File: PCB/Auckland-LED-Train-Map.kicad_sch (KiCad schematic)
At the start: 173 parts, among them U3 Connector, USB-TYPE-C-16P, U4 ESP32-C3FH4, X1 40MHz, 15pF

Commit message: Long Version Checkpoint
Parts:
- removed C1, C18, C22, C8: 4.7uF, PCM_JLCPCB:C_0402, symbol PCM_JLCPCB-Capacitors:0402,4.7uF
- removed C10: 2.7pF, PCM_JLCPCB:C_0402, symbol PCM_JLCPCB-Capacitors:0402,2.7pF
- removed C13: 1pF, PCM_JLCPCB:C_0402, symbol PCM_JLCPCB-Capacitors:0402,1pF
- removed C14: 22uF, PCM_JLCPCB:C_0603, symbol PCM_JLCPCB-Capacitors:0603,22uF
- removed C17: 100nF, PCM_JLCPCB:C_0402, symbol PCM_JLCPCB-Capacitors:0402,100nF
- removed C19: 10uF, PCM_JLCPCB:C_0402, symbol PCM_JLCPCB-Capacitors:0402,10uF
- removed C9: 4.7pF, PCM_JLCPCB:C_0402, symbol PCM_JLCPCB-Capacitors:0402,4.7pF
- removed D10, D100, D101, D102, D103, D104, D11, D12, D13, D14, D15, D16, D17, D18, D19, D2, D20, D200, D201, D202, D203, D204, D205, D206, D207, D208, D209, D21, D210, D211, D212, D213, D214, D215, D216, D217, D218, D22, D23, D24, D25, D26, D27, D28, D29, D3, D30, D31, D32, D33, D34, D35, D36, D37, D38, D39, D4, D40, D41, D42, D43, D44, D45, D46, D47, D48, D49, D5, D50, D51, D52, D53, D54, D55, D56, D57, D58, D59, D6, D60, D61, D62, D63, D64, D65, D66, D67, D68, D69, D7, D70, D71, D72, D73, D74, D75, D76, D77, D78, D79, D8, D80, D81, D82, D83, D84, D85, D86, D87, D88, D89, D9, D90, D91, D92, D93, D94, D95, D96, D97, D98, D99: WS2812B, PCM_JLCPCB:LED-SMD_4P-L1.6-W1.5_XL-1615RGBC-WS2812B, symbol PCM_JLCPCB-Extended:LED, WS2812B, 1615
- removed R1: 510Ω, PCM_JLCPCB:R_0402, symbol PCM_JLCPCB-Resistors:0402,510Ω
- removed R10: 47kΩ, PCM_JLCPCB:R_0402, symbol PCM_JLCPCB-Resistors:0402,47kΩ
- removed R11: 1kΩ, PCM_JLCPCB:R_0402, symbol PCM_JLCPCB-Resistors:0402,1kΩ
- removed R12: 68kΩ, PCM_JLCPCB:R_0402, symbol PCM_JLCPCB-Resistors:0402,68kΩ
- removed R13: 15kΩ, PCM_JLCPCB:R_0402, symbol PCM_JLCPCB-Resistors:0402,15kΩ
- removed R5: 0Ω, PCM_JLCPCB:R_0402, symbol PCM_JLCPCB-Resistors:0402,0Ω
- removed RT1: 47kΩ,4050, JLCPCB-Kicad-Footprints:RT_0402, symbol JLCPCB-Variable-Resistors:NTC,47kΩ,4050,0402
- added C1: 10uF, PCM_JLCPCB:C_0603, symbol PCM_JLCPCB-Capacitors:0603,10uF
- added C2, C21, C22, C6: 100nF, PCM_JLCPCB:C_0402, symbol PCM_JLCPCB-Capacitors:0402,100nF
- added C23, C26, C29, C32, C4, C5, C7: 10uF, PCM_JLCPCB:C_0402, symbol PCM_JLCPCB-Capacitors:0402,10uF
- added C24, C25, C27, C28, C30, C31, C33, C34: 220nF, PCM_JLCPCB:C_0402, symbol PCM_JLCPCB-Capacitors:0402,220nF
- added C35: 1uF, PCM_JLCPCB:C_0402, symbol PCM_JLCPCB-Capacitors:0402,1uF
- added C36, C37: 1.5pF, PCM_JLCPCB:C_0402, symbol PCM_JLCPCB-Capacitors:0402,1.5pF
- added D1: MMSZ5227B, PCM_JLCPCB:D_SOD-123, symbol PCM_JLCPCB-Diodes:Zener,MMSZ5227B
- added D3: SRV05-4A, PCM_JLCPCB:SOT-23-6_L2.9-W1.6-P0.95-LS2.9-BL, symbol PCM_JLCPCB-Diode-Packages:Package, SRV05-4A_C20615829
- added D4, D5: MM1W5V6, PCM_JLCPCB:D_SOD-123, symbol PCM_JLCPCB-Diodes:Zener,MM1W5V6
- added D6, D7: SS54, PCM_JLCPCB:D_SMA, symbol PCM_JLCPCB-Diodes:Schottky,SS54
- added F1: Polyfuse, Fuse:Fuse_0805_2012Metric_Pad1.15x1.40mm_HandSolder, symbol Device:Polyfuse
- added J1: Conn_01x06_Socket, Connector_PinHeader_2.54mm:PinHeader_1x06_P2.54mm_Vertical, symbol Connector:Conn_01x06_Socket
- added Q1: HL3415A, PCM_JLCPCB:Q_SOT-23, symbol PCM_JLCPCB-Transistors:PMOS,HL3415A
- added Q2: MMBT3904, PCM_JLCPCB:Q_SOT-23, symbol PCM_JLCPCB-Transistors:NPN,MMBT3904
- added R10, R15: 100Ω, PCM_JLCPCB:R_0402, symbol PCM_JLCPCB-Resistors:0402,100Ω
- added R11: 0Ω, PCM_JLCPCB:R_0402, symbol PCM_JLCPCB-Resistors:0402,0Ω
- added R16: 100kΩ, PCM_JLCPCB:R_0402, symbol PCM_JLCPCB-Resistors:0402,100kΩ
- added R17: 10kΩ, PCM_JLCPCB:R_0402, symbol PCM_JLCPCB-Resistors:0402,10kΩ
- added R18: 1kΩ, PCM_JLCPCB:R_0402, symbol PCM_JLCPCB-Resistors:0402,1kΩ
- added R19, R20: 5.1kΩ, PCM_JLCPCB:R_0402, symbol PCM_JLCPCB-Resistors:0402,5.1kΩ
- added R21, R8: 0Ω, PCM_JLCPCB:R_1206, symbol PCM_JLCPCB-Resistors:1206,0Ω
- added R7: 750Ω, PCM_JLCPCB:R_1206, symbol PCM_JLCPCB-Resistors:1206,750Ω
- added TP1: NAL-NIMT_LED, Custom_Footprints:TestPoint_Pad_D2.0mm, symbol Connector:TestPoint
- added TP2: NAL-NIMT_MCU, Custom_Footprints:TestPoint_Pad_D2.0mm, symbol Connector:TestPoint
- added TP3: STRAND-MNK_MCU, Custom_Footprints:TestPoint_Pad_D2.0mm, symbol Connector:TestPoint
- added TP4: STRAND-MNK_LED, Custom_Footprints:TestPoint_Pad_D2.0mm, symbol Connector:TestPoint
- added TP5: PMOS_Gate, Custom_Footprints:TestPoint_Pad_D2.0mm, symbol Connector:TestPoint
- added TP6: LED_+5V, Custom_Footprints:TestPoint_Pad_D2.0mm, symbol Connector:TestPoint
- added TP7: NPN_Gate, Custom_Footprints:TestPoint_Pad_D2.0mm, symbol Connector:TestPoint
- added U1: XC6206P332MR, PCM_JLCPCB:SOT-23-3_L2.9-W1.6-P1.90-LS2.8-BR, symbol PCM_JLCPCB-Power:LDO, 3.3V, 0.2A
- added U3: SN74LVC4245APWR, PCM_JLCPCB:TSSOP-24_L7.8-W4.4-P0.65-LS6.4-BL, symbol PCM_JLCPCB-ICs:Level Shifter, 8 Channel, TSN74LVC4245APWR
- added U5: Connector, USB-TYPE-C-16P, PCM_JLCPCB:TYPE-C-SMD_HX-TYPE-C-16PIN, symbol PCM_JLCPCB-Extended:Connector, USB-TYPE-C-16P
- AE1: footprint Inverted_F_Antenna_2.4Ghz_1.0mmPCB_TI_CC2430DB:Inverted_F_Antenna_2.4Ghz_1.0mmPCB_TI_CC2430DB.pretty -> Custom_Footprints:Inverted_F_Antenna_2.4Ghz_1.0mmPCB_TI_CC2430DB.pretty
- C10: renamed from C2; Stock 21965782 -> 20577604
- C11: renamed from C3; Stock 21965782 -> 20577604
- C12: renamed from C5; Stock 2758866 -> 2162276
- C13: renamed from C6; Stock 7581604 -> 6607844
- C14: renamed from C12; Stock 21965782 -> 20577604
- C18: renamed from C4; Stock 7581604 -> 6607844
- C19: renamed from C15; Stock 727564 -> 680404
- C20: renamed from C16; Stock 727564 -> 680404
- C3: renamed from C21; Stock 21965782 -> 20577604
- C8: renamed from C7; Stock 3016191 -> 1595146
- C9: renamed from C11; Stock 21965782 -> 20577604
- D2: renamed from D1; Stock 2247940 -> 2161099
- FB1: Stock 155765 -> 233758
- L1: renamed from L3; Stock 66961 -> 55146
- L2: renamed from L4; Stock 66961 -> 55146
- R1: renamed from R8; Stock 11020501 -> 14335141
- R12: renamed from R16; Stock 652462 -> 859567
- R13: renamed from R14; Stock 2165496 -> 3549665
- R14: renamed from R15; Stock 2165496 -> 3549665
- R2: renamed from R7; Stock 11020501 -> 14335141
- R3: renamed from R2; Stock 11020501 -> 14335141
- R4: renamed from R6; Stock 4267977 -> 6150463
- R5: renamed from R3; Stock 7578144 -> 6497432
- R6: renamed from R4; Stock 7578144 -> 6497432
- R9: Stock 7578144 -> 6497432
- renumbered U4 to U2, U3 to U4
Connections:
- net +3V3: now also C22.1, C4.1, C5.1, C6.1, D1.1, U1.2 (VOUT), U3.23 (VCCB(3V)), U3.24 (VCCB(3V)); no longer C10.1, C11.1, C12.1, C13.1, U2.11 (VDD3P3_RTC), U2.17 (VDD3P3_CPU), U2.31 (VDDA), U2.32 (VDDA)
- net Antenna: now also C36.1
- net BOOT_IO9: now also J1.4 (Pin_4)
- net D+: now also D3.3 (I/O), D3.4 (I/O)
- net D-: now also D3.1 (I/O), D3.6 (I/O)
- net GND: now also C1.2, C2.2, C21.2, C22.2, C23.2, C24.2, C25.2, C26.2, C27.2, C28.2, C29.2, C30.2, C31.2, C32.2, C33.2, C34.2, C35.2, C36.2, C37.2, C4.2, C5.2, C6.2, C7.2, D1.2, D3.2 (VN), D4.2, D5.2, J1.2 (Pin_2), Q2.2 (E), R11.1, R17.2, R19.2, R20.2, U1.1 (GND), U3.11 (GND), U3.12 (GND), U3.13 (GND), U5.A12B1 (GND), U5.B12A1 (GND), U5.S1 (SHIELD)
- net MCU_RX: now also J1.5 (Pin_5), R8.2
- net MCU_TX: now also J1.6 (Pin_6), R7.1
- net Reset: now also J1.3 (Pin_3)
- net VBUS: now also C1.1, C2.1, C21.1, D3.5 (VP), D5.1, F1.2, J1.1 (Pin_1), Q1.2 (S), R16.1, U1.3 (VIN), U3.1 (VCCA(5V))
- net at AE1.1 (A), L1.2, L2.2: now also C37.1
- net at U2.28 (U0TXD): now also R7.2
- net at C8.1, C9.1, FB1.2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: now also C10.1, C11.1, U2.11 (VDD3P3_RTC), U2.17 (VDD3P3_CPU), C7.1, R21.1
- net at U2.27 (U0RXD): now also R8.1
- net NAL-NIMT_MCU: now reaches U2.8 (GPIO3)
- net NAL-NIMT_MCU: now also TP2.1, U3.21 (B1)
- net at U4.A9B4 (VBUS), U4.B9A4 (VBUS): now also D6.2; no longer D2.2
- new net: C35.1, Q2.1 (B), R18.2, TP7.1
- new net: Q1.1 (G), Q2.3 (C), R16.2, TP5.1
- new net: C12.1, C13.1, R21.2, U2.31 (VDDA), U2.32 (VDDA)
- new net: R20.1, U5.A5 (CC1)
- new net: D2.2, D6.1, D7.1, F1.1
- new net: D7.2, U5.A9B4 (VBUS), U5.B9A4 (VBUS)
- new net: R19.1, U5.B5 (CC2)
- new net: R11.2, U3.2 (DIR)
- new net: R10.2, U3.3 (A1)
- new net: R15.2, U3.10 (A8)
- new net +5V: C23.1, C24.1, C25.1, C26.1, C27.1, C28.1, C29.1, C30.1, C31.1, C32.1, C33.1, C34.1, D4.1, Q1.3 (D), TP6.1
- new net LED_+5V_EN_Active_High: R17.1, R18.1
- new net LVL_Shifter_EN_Active_Low: U3.22 (OE#)
- new net NAL-NIMT-1: R10.1, TP1.1
- new net STRAND-MNK-1: R15.1, TP4.1
- new net STRAND-MNK_MCU: TP3.1, U3.14 (B8)
- no-connect marks 4 -> 16
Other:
- added sheet NAL-NIMT-1 (NAL-NIMT-1.kicad_sch)
- added sheet STRAND-MNK-1 (STRAND-MNK-1.kicad_sch)
- note added: "3.42~3.78V"
- moved on the sheet: AE1, C14, C3, C8, H1, H2, H3, H4, PN1, R4, U4

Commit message: PCB Checkpoint
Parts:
- removed C23, C26, C29, C32, C7, C8: 10uF, PCM_JLCPCB:C_0402, symbol PCM_JLCPCB-Capacitors:0402,10uF
- removed C24, C25, C27, C28, C30, C31, C33, C34: 220nF, PCM_JLCPCB:C_0402, symbol PCM_JLCPCB-Capacitors:0402,220nF
- removed C9: 100nF, PCM_JLCPCB:C_0402, symbol PCM_JLCPCB-Capacitors:0402,100nF
- removed FB1: ~, PCM_JLCPCB:FB_0805, symbol PCM_JLCPCB-Inductors:Ferrite,0805,(2)
- removed R9: 0Ω, PCM_JLCPCB:R_0402, symbol PCM_JLCPCB-Resistors:0402,0Ω
- removed TP3: STRAND-MNK_MCU, Custom_Footprints:TestPoint_Pad_D2.0mm, symbol Connector:TestPoint
- added C15: 100nF, PCM_JLCPCB:C_0402, symbol PCM_JLCPCB-Capacitors:0402,100nF
- added C7: 1uF, PCM_JLCPCB:C_0402, symbol PCM_JLCPCB-Capacitors:0402,1uF
- added L3, L4: 3.9nH,300mA, PCM_JLCPCB:L_0402, symbol PCM_JLCPCB-Inductors:3.9nH,300mA
- added L5: 15nH,300mA, PCM_JLCPCB:L_0402, symbol PCM_JLCPCB-Inductors:15nH,300mA
- added TP8: STRAND-MNK_MCU, Custom_Footprints:TestPoint_Pad_D2.0mm, symbol Connector:TestPoint
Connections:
- net +3V3: now also L3.1, L4.1
- net GND: now also C15.2, C7.2
- net STRAND-MNK_MCU: now also U3.17 (B5), TP8.1; no longer U3.14 (B8)
- net at C10.1, C11.1, R21.1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: now also C15.1, C7.1, L3.2, L4.2
- net at U2.30 (XTAL_P): now also L5.2
- net at R15.2: now also U3.7 (A5); no longer U3.10 (A8)
- net at C20.1, X1.1 (OSC): now also L5.1
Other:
- moved on the sheet: R15

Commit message: - Remove JLCPCB Outputs - V1 RC1
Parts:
- removed R21, R8: 0Ω, PCM_JLCPCB:R_1206, symbol PCM_JLCPCB-Resistors:1206,0Ω
- removed R7: 750Ω, PCM_JLCPCB:R_1206, symbol PCM_JLCPCB-Resistors:1206,750Ω
- added C16: 100nF, PCM_JLCPCB:C_0402, symbol PCM_JLCPCB-Capacitors:0402,100nF
- added C8: 10uF, PCM_JLCPCB:C_0402, symbol PCM_JLCPCB-Capacitors:0402,10uF
- added D8, D9: Green, PCM_JLCPCB:D_0805, symbol PCM_JLCPCB-Diodes:LED,0805,Green
- added R22, R9: 47kΩ, PCM_JLCPCB:R_0402, symbol PCM_JLCPCB-Resistors:0402,47kΩ
- added R7: 510Ω, PCM_JLCPCB:R_0402, symbol PCM_JLCPCB-Resistors:0402,510Ω
- added S1, S2, S3: Tactile Button, 160gf, PCM_JLCPCB:SW-SMD_4P-L5.1-W5.1-P3.70-LS6.5-TL-2, symbol PCM_JLCPCB-Connectors_Buttons:Tactile Button, 160gf
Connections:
- net +3V3: now also C10.1, C11.1, C12.1, C13.1, U2.11 (VDD3P3_RTC), U2.17 (VDD3P3_CPU), U2.31 (VDDA), U2.32 (VDDA), C8.1, D8.2
- net GND: now also C16.2, C8.2, R22.2, R9.2, S1.3 (C), S1.4 (D), S2.3 (C), S2.4 (D), S3.3 (C), S3.4 (D)
- net LVL_Shifter_EN_Active_Low: now also U2.8 (GPIO3)
- net MCU_RX: now also U2.27 (U0RXD)
- net MCU_TX: now also R7.1
- net NAL-NIMT_MCU: now also U2.9 (MTMS); no longer U2.8 (GPIO3)
- net STRAND-MNK_MCU: now also U2.10 (MTDI)
- net VDD_SPI: now also C16.1
- net MODE_BUTTON: now reaches R2.2, U2.14 (GPIO8)
- net MODE_BUTTON: now also S1.1 (A), S1.2 (B)
- net at C15.1, C7.1, L3.2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: no longer C10.1, C11.1, U2.11 (VDD3P3_RTC), U2.17 (VDD3P3_CPU)
- net -BRIGHTNESS_BUTTON: now reaches U2.12 (MTCK)
- net -BRIGHTNESS_BUTTON: now also S3.1 (A), S3.2 (B)
- net +BRIGHTNESS_BUTTON: now reaches U2.13 (MTDO)
- net +BRIGHTNESS_BUTTON: now also S2.1 (A), S2.2 (B)
- net WIFI_LED: now reaches U2.16 (GPIO10)
- net WIFI_LED: now also D9.2
- net at U2.28 (U0TXD): now also R7.2
- new net: D9.1, R22.1
- new net: D8.1, R9.1
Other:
- note added: "Power"
- moved on the sheet: C6, L3, L4, R1, R2, R3

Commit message: - V1 RC2 - Add icons
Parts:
- added C9: 10uF, PCM_JLCPCB:C_0402, symbol PCM_JLCPCB-Capacitors:0402,10uF
- added D10, D11: Red, PCM_JLCPCB:D_0805, symbol PCM_JLCPCB-Diodes:LED,0805,Red
- added D12: Green, PCM_JLCPCB:D_0805, symbol PCM_JLCPCB-Diodes:LED,0805,Green
- added R21, R8: 15kΩ, PCM_JLCPCB:R_0402, symbol PCM_JLCPCB-Resistors:0402,15kΩ
- added R23: 47kΩ, PCM_JLCPCB:R_0402, symbol PCM_JLCPCB-Resistors:0402,47kΩ
- D2: footprint PCM_JLCPCB:D_0603 -> PCM_JLCPCB:D_0805; symbol PCM_JLCPCB-Diodes:LED,0603,Red -> PCM_JLCPCB-Diodes:LED,0805,Red; Category Optocouplers & LEDs & Infrared,Light Emitting Diodes (LED) -> Optoelectronics,Light Emitting Diodes (LED); Diode Configuration (none) -> Independent Diode; Dominant Wavelength (none) -> 615nm~630nm; Emitted Color (none) -> Red; Forward Current (none) -> 25mA; Forward Voltage (VF) (none) -> 1.6V~2.6V; LCSC C2286 -> C84256; Lens Color (none) -> Colorless Transparent Lens; Luminous Intensity (none) -> 67mcd~195mcd; Manufacturer Hubei KENTO Elec -> Foshan NationStar Optoelectronics; Operating Temperature (none) -> -30°C~+85°C; Part KT-0603R -> NCD0805R1; Power Dissipation (none) -> 65mW; Price 0.009USD -> 0.016USD; Stock 2161099 -> 3045161; Viewing Angle (none) -> 130°
- R12: value 3.3kΩ -> 15kΩ; symbol PCM_JLCPCB-Resistors:0402,3.3kΩ -> PCM_JLCPCB-Resistors:0402,15kΩ; LCSC C25890 -> C25756; Part 0402WGF3301TCE -> 0402WGF1502TCE; Resistance 3.3kΩ -> 15kΩ; Stock 859567 -> 534593
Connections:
- net +3V3: now also C9.1
- net GND: now also U3.10 (A8), U3.14 (B8), U3.15 (B7), U3.16 (B6), U3.17 (B5), U3.18 (B4), U3.19 (B3), U3.5 (A3), U3.6 (A4), U3.7 (A5), U3.8 (A6), U3.9 (A7), C9.2, D10.2, D11.2, R23.2
- net LED_+5V_EN_Active_High: now also U2.9 (MTMS)
- net LVL_Shifter_EN_Active_Low: now also U2.4 (GPIO0/XTAL_32K_P); no longer U2.8 (GPIO3)
- net NAL-NIMT_MCU: now also U2.8 (GPIO3), U3.20 (B2); no longer U2.9 (MTMS), U3.21 (B1)
- net STRAND-MNK_MCU: now also U2.5 (GPIO1/XTAL_32K_N), U3.21 (B1); no longer U2.10 (MTDI), U3.17 (B5)
- net WIFI_LED: now also R8.1
- net at R10.2: now also U3.4 (A2); no longer U3.3 (A1)
- net at R15.2: now also U3.3 (A1); no longer U3.7 (A5)
- net BOOT_IO9 renamed BOOT_IO9_BUTTON
- net BOOT_IO9_BUTTON: now also S1.1 (A), S1.2 (B)
- net MODE_BUTTON: no longer names the net of R2.2, U2.14 (GPIO8)
- net MODE_BUTTON: no longer S1.1 (A), S1.2 (B)
- new net: D12.1, R23.1
- new net: D10.1, R8.2
- new net: D11.1, R21.2
- new net CONFIG_LED: D12.2, R21.1, U2.10 (MTDI)
- no-connect marks 16 -> 14
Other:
- note removed: "Power"
- moved on the sheet: AE1, C1, C10, C11, C12, C13, C14, C15, C16, C18, C19, C2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

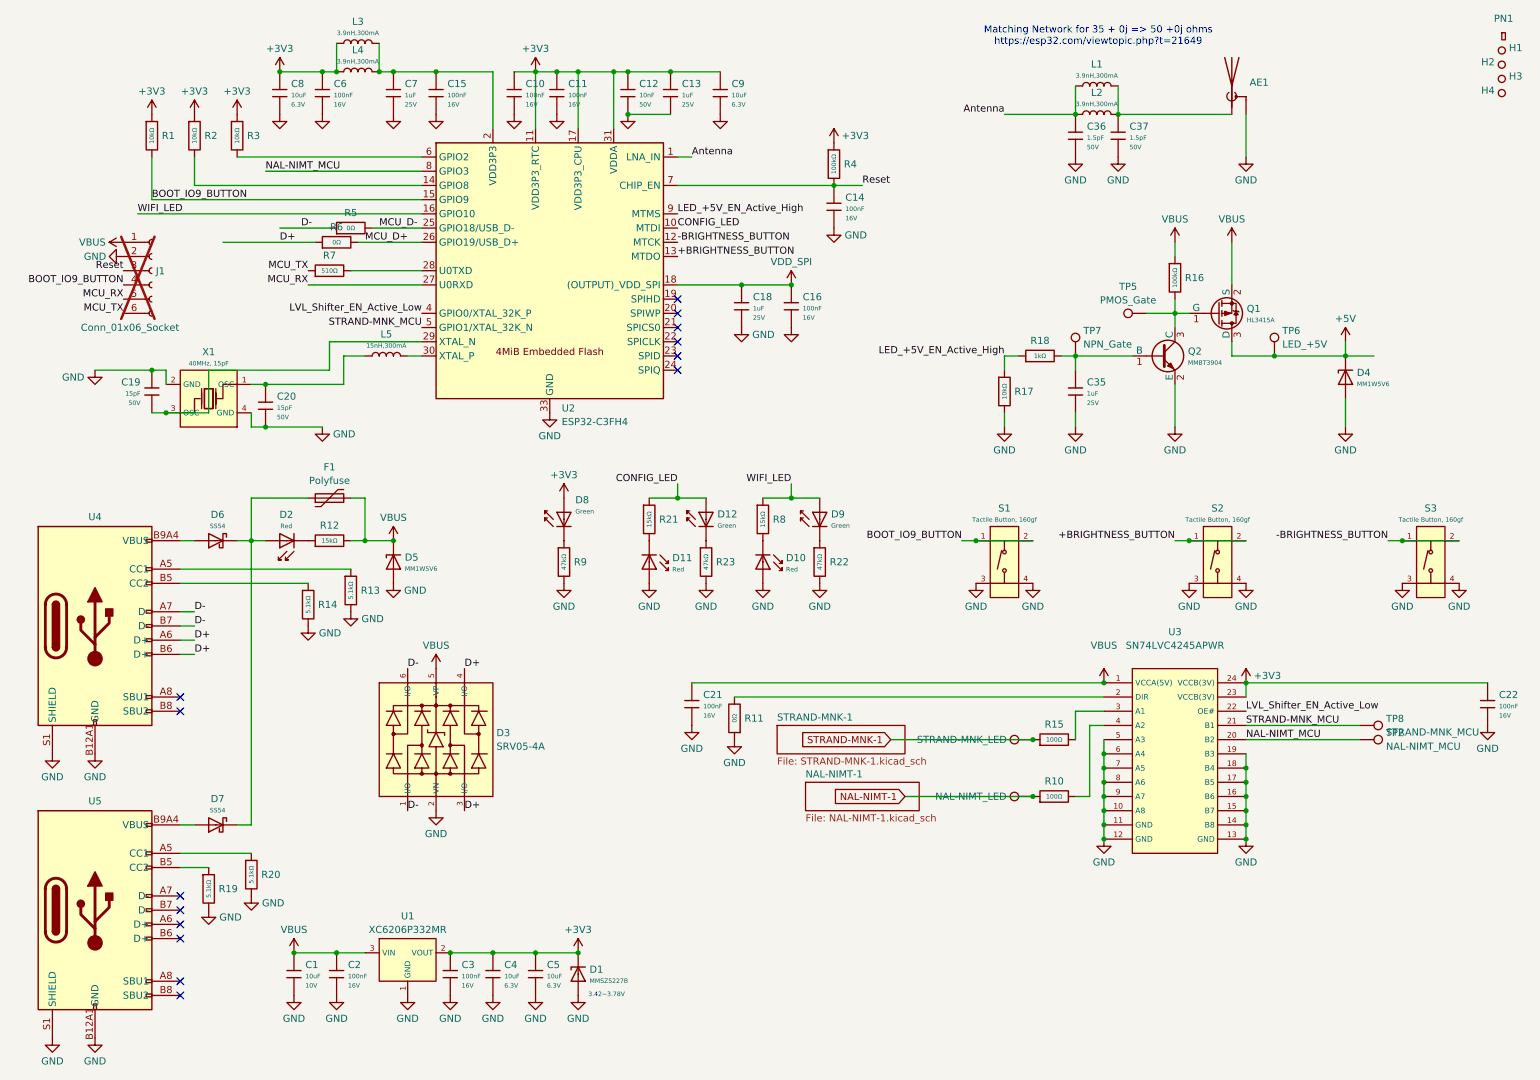
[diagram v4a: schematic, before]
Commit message: - Add Readme - V1 RC3 PCB - Tidy up Schematic - Add Datasheets
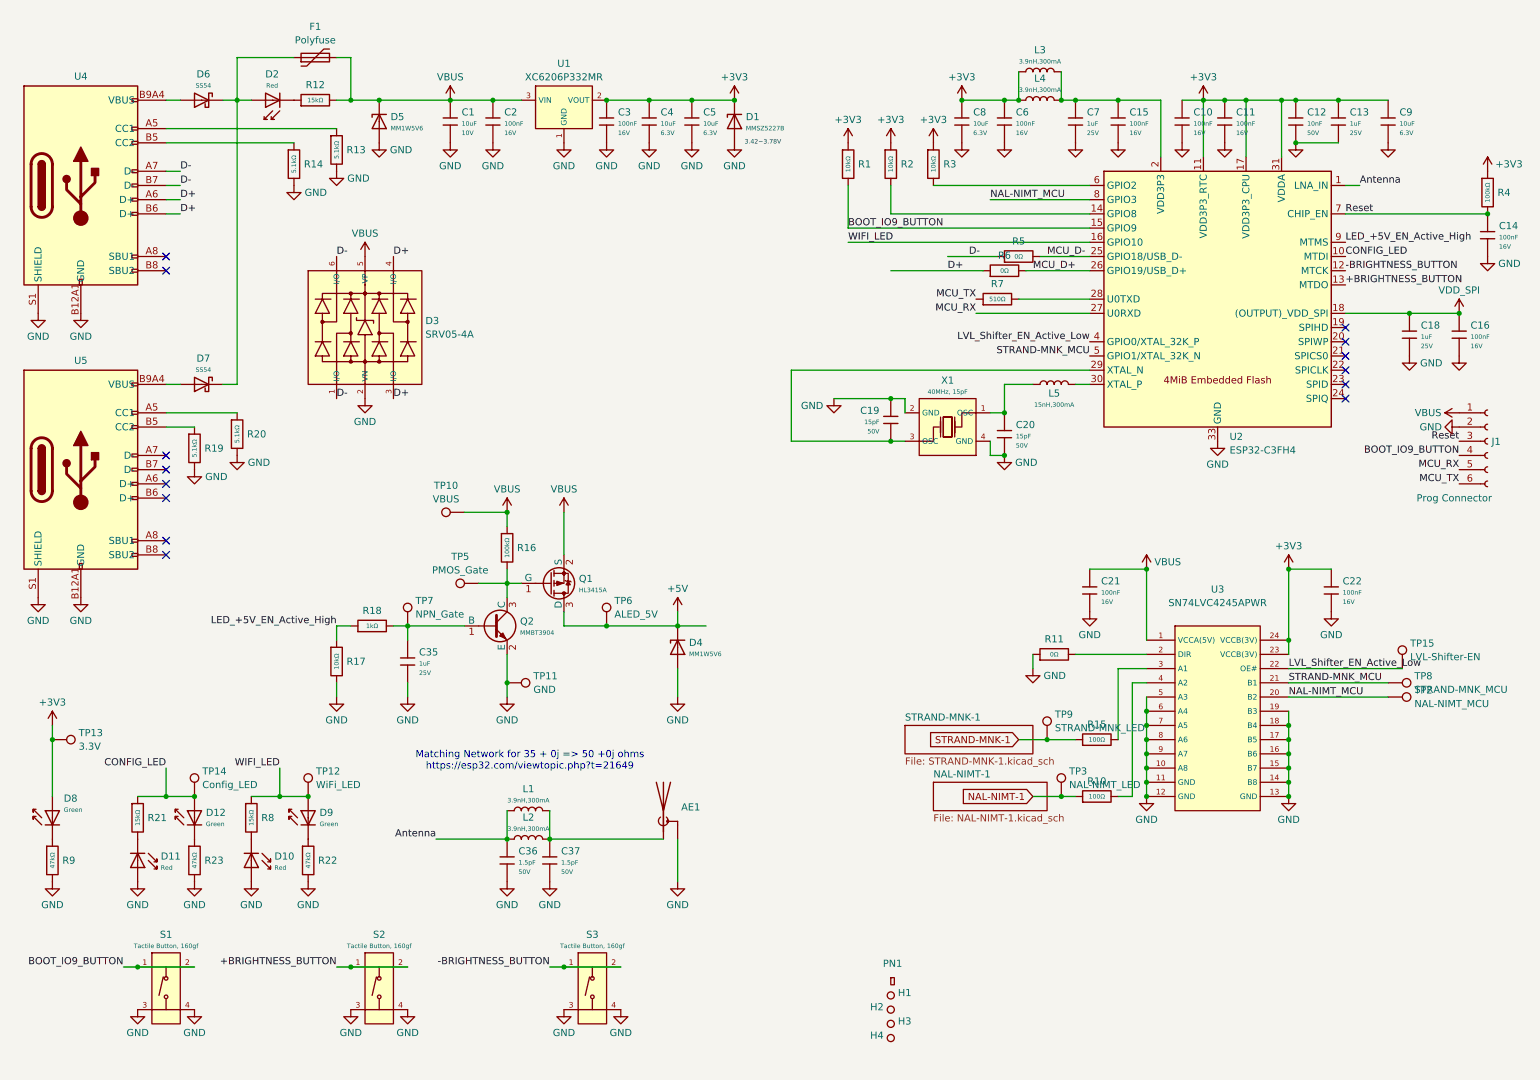
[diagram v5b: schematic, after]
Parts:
- removed TP1: NAL-NIMT_LED, Custom_Footprints:TestPoint_Pad_D2.0mm, symbol Connector:TestPoint
- removed TP4: STRAND-MNK_LED, Custom_Footprints:TestPoint_Pad_D2.0mm, symbol Connector:TestPoint
- added TP10: VBUS, Custom_Footprints:TestPoint_Pad_D1.0mm, symbol Connector:TestPoint
- added TP11: GND, Custom_Footprints:TestPoint_Pad_D1.0mm, symbol Connector:TestPoint
- added TP12: WiFi_LED, Custom_Footprints:TestPoint_Pad_D1.0mm, symbol Connector:TestPoint
- added TP13: 3.3V, Custom_Footprints:TestPoint_Pad_D1.0mm, symbol Connector:TestPoint
- added TP14: Config_LED, Custom_Footprints:TestPoint_Pad_D1.0mm, symbol Connector:TestPoint
- added TP15: LVL-Shifter-EN, Custom_Footprints:TestPoint_Pad_D1.0mm, symbol Connector:TestPoint
- added TP3: NAL-NIMT_LED, Custom_Footprints:TestPoint_Pad_D1.0mm, symbol Connector:TestPoint
- added TP9: STRAND-MNK_LED, Custom_Footprints:TestPoint_Pad_D1.0mm, symbol Connector:TestPoint
- J1: value Conn_01x06_Socket -> Prog Connector; footprint Connector_PinHeader_2.54mm:PinHeader_1x06_P2.54mm_Vertical -> Custom_Footprints:Prog Connector; now fitted
- TP2, TP5, TP7, TP8: footprint Custom_Footprints:TestPoint_Pad_D2.0mm -> Custom_Footprints:TestPoint_Pad_D1.0mm
- TP6: value LED_+5V -> ALED_5V; footprint Custom_Footprints:TestPoint_Pad_D2.0mm -> Custom_Footprints:TestPoint_Pad_D1.0mm
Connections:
- net +3V3: now also TP13.1
- net CONFIG_LED: now also TP14.1
- net GND: now also TP11.1
- net LVL_Shifter_EN_Active_Low: now also TP15.1
- net NAL-NIMT-1: now also TP3.1
- net STRAND-MNK-1: now also TP9.1
- net VBUS: now also TP10.1
- net WIFI_LED: now also TP12.1
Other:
- title: Auckland LED Train Map -> Auckland Train Network Live Map
- moved on the sheet: AE1, C1, C10, C11, C12, C13, C14, C15, C16, C18, C19, C2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
